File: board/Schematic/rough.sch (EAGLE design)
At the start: 2 parts

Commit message: trying to fix docs glitch
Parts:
- added C1, C2: 10uF, capacitor-wima:C5/3.5
- added C3: 1uF, capacitor-wima:C5/3.5
- added INDUCTOR: INDUCTOR, Test:INDUCTOR
- R1: device rcl:R-EU_M3216 -> resistor:R-US_R1206
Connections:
- new net GND: C1.2, C2.1, U$1.PAD, U$1.TIMER
- new net N$2: C2.2, U$1.BAT
- new net N$3: INDUCTOR.PIN1, R1.1, U$1.SENSE
- new net N$4: C3.1, INDUCTOR.PIN2, U$1.SW
- new net N$5: C3.2, U$1.BOOST
- net N$1: now also C1.1, U$1.SHDN, U$1.VIN; no longer R1.1
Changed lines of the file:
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@@
 <setting verticaltext="up"/>
 </settings>
-<grid distance="0.05" unitdist="mm" unit="mm" style="lines" multiple="1" display="no" altdistance="0.01" altunitdist="inch" altunit="inch"/>
+<grid distance="0.1" unitdist="inch" unit="inch" style="lines" multiple="1" display="yes" altdistance="0.01" altunitdist="inch" altunit="inch"/>
 <layers>
 <layer number="1" name="Top" color="4" fill="1" visible="no" active="no"/>
@@
 <layer number="91" name="Nets" color="2" fill="1" visible="yes" active="yes"/>
 <layer number="92" name="Busses" color="1" fill="1" visible="yes" active="yes"/>
-<layer number="93" name="Pins" color="2" fill="1" visible="yes" active="yes"/>
+<layer number="93" name="Pins" color="2" fill="1" visible="no" active="yes"/>
 <layer number="94" name="Symbols" color="4" fill="1" visible="yes" active="yes"/>
 <layer number="95" name="Names" color="7" fill="1" visible="yes" active="yes"/>
@@
 </classes>
 <parts>
-<part name="U$1" library="Test" deviceset="LT3652" device=""/>
-<part name="R1" library="rcl" deviceset="R-EU_" device="M3216" value="0.05"/>
 <part name="SUPPLY1" library="supply2" deviceset="GND" device=""/>
-<part name="SUPPLY2" library="supply2" deviceset="GND" device=""/>
 <part name="SUPPLY3" library="supply2" deviceset="GND" device=""/>
 <part name="SUPPLY4" library="supply2" deviceset="GND" device=""/>
+<part name="C1" library="capacitor-wima" deviceset="C" device="5/3.5" value="10uF"/>
+<part name="C2" library="capacitor-wima" deviceset="C" device="5/3.5" value="10uF"/>
+<part name="C3" library="capacitor-wima" deviceset="C" device="5/3.5" value="1uF"/>
+<part name="INDUCTOR" library="Test" deviceset="INDUCTOR" device=""/>
+<part name="U$1" library="Test" deviceset="LT3652" device=""/>
+<part name="SUPPLY2" library="supply2" deviceset="GND" device=""/>
+<part name="SUPPLY5" library="supply2" deviceset="GND" device=""/>
+<part name="SUPPLY6" library="supply2" deviceset="GND" device=""/>
+<part name="SUPPLY7" library="supply2" deviceset="GND" device=""/>
+<part name="R1" library="resistor" deviceset="R-US_" device="R1206" value="0.05"/>
 </parts>
 <sheets>
@@
 </plain>
 <instances>
-<instance part="U$1" gate="G$2" x="53.34" y="48.26" rot="R270"/>
-<instance part="R1" gate="G$1" x="85.1" y="50.65"/>
-<instance part="SUPPLY1" gate="GND" x="33.02" y="33.02"/>
-<instance part="SUPPLY2" gate="GND" x="53.49" y="22.95"/>
+<instance part="SUPPLY1" gate="GND" x="12.7" y="73.66"/>
 <instance part="SUPPLY3" gate="GND" x="111.76" y="12.7"/>
-<instance part="SUPPLY4" gate="GND" x="71.12" y="76.2"/>
+<instance part="SUPPLY4" gate="GND" x="35.56" y="45.72"/>
+<instance part="C1" gate="G$1" x="12.7" y="83.82"/>
+<instance part="C2" gate="G$1" x="86.36" y="48.26" rot="R180"/>
+<instance part="C3" gate="G$1" x="78.74" y="71.12"/>
+<instance part="INDUCTOR" gate="G$1" x="93.98" y="71.12" rot="R90"/>
+<instance part="U$1" gate="G$2" x="53.34" y="55.88" rot="R270"/>
+<instance part="SUPPLY2" gate="GND" x="53.34" y="33.02"/>
+<instance part="SUPPLY5" gate="GND" x="53.34" y="25.4"/>
+<instance part="SUPPLY6" gate="GND" x="45.72" y="25.4"/>
+<instance part="SUPPLY7" gate="GND" x="86.36" y="43.18"/>
+<instance part="R1" gate="G$1" x="88.9" y="58.42"/>
 </instances>
 <busses>
@@
 <net name="N$1" class="0">
 <segment>
-<pinref part="R1" gate="G$1" pin="1"/>
-<wire x1="71.12" y1="50.8" x2="80.02" y2="50.65" width="0.1524" layer="91"/>
+<wire x1="12.7" y1="88.9" x2="33.02" y2="88.9" width="0.1524" layer="91"/>
+<pinref part="C1" gate="G$1" pin="1"/>
+<wire x1="33.02" y1="88.9" x2="104.14" y2="88.9" width="0.1524" layer="91"/>
+<wire x1="12.7" y1="86.36" x2="12.7" y2="88.9" width="0.1524" layer="91"/>
+<wire x1="33.02" y1="88.9" x2="33.02" y2="63.5" width="0.1524" layer="91"/>
+<junction x="33.02" y="88.9"/>
+<pinref part="U$1" gate="G$2" pin="SHDN"/>
+<wire x1="33.02" y1="63.5" x2="33.02" y2="58.42" width="0.1524" layer="91"/>
+<wire x1="33.02" y1="58.42" x2="38.1" y2="58.42" width="0.1524" layer="91"/>
+<pinref part="U$1" gate="G$2" pin="VIN"/>
+<wire x1="38.1" y1="63.5" x2="33.02" y2="63.5" width="0.1524" layer="91"/>
+<junction x="33.02" y="63.5"/>
+</segment>
+</net>
+<net name="GND" class="0">
+<segment>
+<pinref part="SUPPLY4" gate="GND" pin="GND"/>
+<pinref part="U$1" gate="G$2" pin="TIMER"/>
+<wire x1="35.56" y1="48.26" x2="38.1" y2="48.26" width="0.1524" layer="91"/>
+</segment>
+<segment>
+<pinref part="SUPPLY1" gate="GND" pin="GND"/>
+<pinref part="C1" gate="G$1" pin="2"/>
+<wire x1="12.7" y1="76.2" x2="12.7" y2="78.74" width="0.1524" layer="91"/>
+</segment>
+<segment>
+<pinref part="U$1" gate="G$2" pin="PAD"/>
+<pinref part="SUPPLY2" gate="GND" pin="GND"/>
+<wire x1="53.34" y1="40.64" x2="53.34" y2="35.56" width="0.1524" layer="91"/>
+</segment>
+<segment>
+<pinref part="C2" gate="G$1" pin="1"/>
+<pinref part="SUPPLY7" gate="GND" pin="GND"/>
 </segment>
 </net>
 <net name="N$2" class="0">
 <segment>
-<wire x1="33" y1="35.6" x2="33" y2="35.9" width="0.1524" layer="91"/>
-<wire x1="33" y1="35.9" x2="36.85" y2="39.75" width="0.1524" layer="91"/>
+<pinref part="U$1" gate="G$2" pin="BAT"/>
+<wire x1="68.58" y1="53.34" x2="86.36" y2="53.34" width="0.1524" layer="91"/>
+<pinref part="C2" gate="G$1" pin="2"/>
+<wire x1="86.36" y1="53.34" x2="93.98" y2="53.34" width="0.1524" layer="91"/>
+<junction x="86.36" y="53.34"/>
 </segment>
 </net>
 <net name="N$3" class="0">
 <segment>
-<wire x1="53.6" y1="26" x2="53.45" y2="26" width="0.1524" layer="91"/>
-<wire x1="53.45" y1="26" x2="53.45" y2="29.75" width="0.1524" layer="91"/>
+<pinref part="U$1" gate="G$2" pin="SENSE"/>
+<pinref part="R1" gate="G$1" pin="1"/>
+<wire x1="68.58" y1="58.42" x2="81.28" y2="58.42" width="0.1524" layer="91"/>
+<pinref part="INDUCTOR" gate="G$1" pin="PIN1"/>
+<wire x1="81.28" y1="58.42" x2="83.82" y2="58.42" width="0.1524" layer="91"/>
+<wire x1="86.36" y1="68.58" x2="81.28" y2="63.5" width="0.1524" layer="91"/>
+<wire x1="81.28" y1="63.5" x2="81.28" y2="58.42" width="0.1524" layer="91"/>
+<junction x="81.28" y="58.42"/>
 </segment>
 </net>
+<net name="N$4" class="0">
+<segment>
+<pinref part="U$1" gate="G$2" pin="SW"/>
+<pinref part="C3" gate="G$1" pin="1"/>
+<wire x1="68.58" y1="63.5" x2="68.58" y2="73.66" width="0.1524" layer="91"/>
+<wire x1="68.58" y1="73.66" x2="78.74" y2="73.66" width="0.1524" layer="91"/>
+<pinref part="INDUCTOR" gate="G$1" pin="PIN2"/>
+<wire x1="78.74" y1="73.66" x2="86.36" y2="73.66" width="0.1524" layer="91"/>
+<junction x="78.74" y="73.66"/>
+</segment>
+</net>
+<net name="N$5" class="0">
+<segment>
+<pinref part="U$1" gate="G$2" pin="BOOST"/>
+<pinref part="C3" gate="G$1" pin="2"/>
+<wire x1="68.58" y1="60.96" x2="78.74" y2="66.04" width="0.1524" layer="91"/>
+</segment>
+</net>

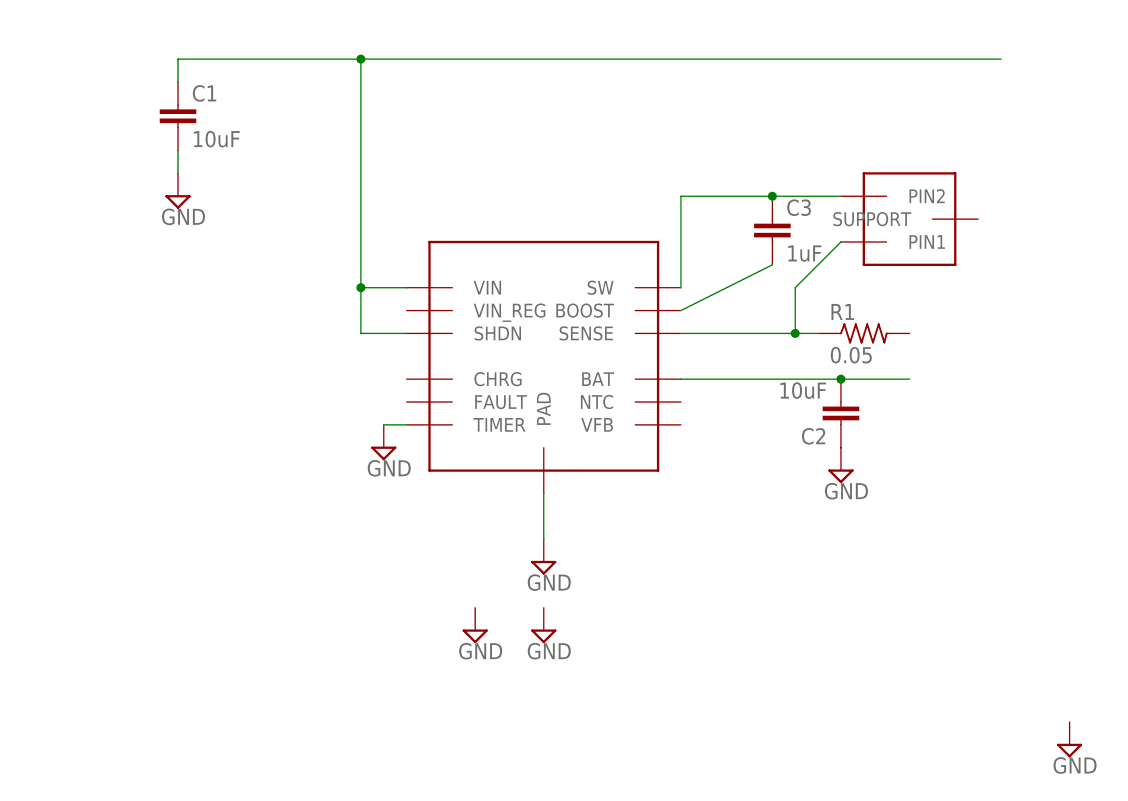
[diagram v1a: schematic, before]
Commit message: diodes added
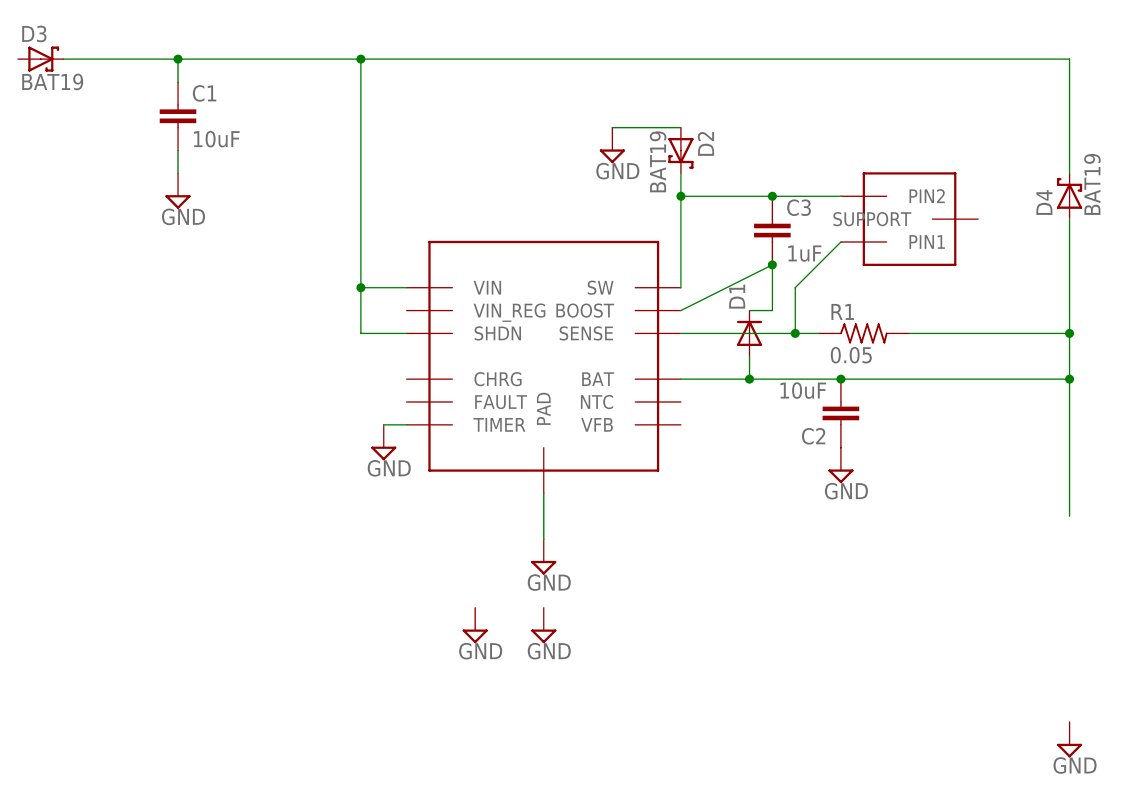
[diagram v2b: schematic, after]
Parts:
- added D1: (no value), diode:DIODE-SOD80C
- added D2, D3, D4: BAT19, diode:BAT19
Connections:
- net GND: now also D2.A
- net N$1: now also D3.C, D4.C
- net N$2: now also D1.A, D4.A, R1.2
- net N$4: now also D2.C
- net N$5: now also D1.C
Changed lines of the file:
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@@
 <setting verticaltext="up"/>
 </settings>
-<grid distance="0.1" unitdist="inch" unit="inch" style="lines" multiple="1" display="yes" altdistance="0.01" altunitdist="inch" altunit="inch"/>
+<grid distance="0.1" unitdist="inch" unit="inch" style="lines" multiple="1" display="no" altdistance="0.01" altunitdist="inch" altunit="inch"/>
 <layers>
 <layer number="1" name="Top" color="4" fill="1" visible="no" active="no"/>
@@
 <part name="SUPPLY7" library="supply2" deviceset="GND" device=""/>
 <part name="R1" library="resistor" deviceset="R-US_" device="R1206" value="0.05"/>
+<part name="D2" library="diode" deviceset="BAT19" device=""/>
+<part name="SUPPLY8" library="supply2" deviceset="GND" device=""/>
+<part name="D1" library="diode" deviceset="DIODE-" device="SOD80C"/>
+<part name="D3" library="diode" deviceset="BAT19" device=""/>
+<part name="D4" library="diode" deviceset="BAT19" device=""/>
 </parts>
 <sheets>
@@
 <instance part="SUPPLY7" gate="GND" x="86.36" y="43.18"/>
 <instance part="R1" gate="G$1" x="88.9" y="58.42"/>
+<instance part="D2" gate="1" x="68.58" y="78.74" rot="R270"/>
+<instance part="SUPPLY8" gate="GND" x="60.96" y="78.74"/>
+<instance part="D1" gate="G$1" x="76.2" y="58.42" rot="R90"/>
+<instance part="D3" gate="1" x="-2.54" y="88.9"/>
+<instance part="D4" gate="1" x="111.76" y="73.66" rot="R90"/>
 </instances>
 <busses>
@@
 <wire x1="12.7" y1="88.9" x2="33.02" y2="88.9" width="0.1524" layer="91"/>
 <pinref part="C1" gate="G$1" pin="1"/>
-<wire x1="33.02" y1="88.9" x2="104.14" y2="88.9" width="0.1524" layer="91"/>
+<wire x1="33.02" y1="88.9" x2="111.76" y2="88.9" width="0.1524" layer="91"/>
 <wire x1="12.7" y1="86.36" x2="12.7" y2="88.9" width="0.1524" layer="91"/>
 <wire x1="33.02" y1="88.9" x2="33.02" y2="63.5" width="0.1524" layer="91"/>
@@
 <wire x1="38.1" y1="63.5" x2="33.02" y2="63.5" width="0.1524" layer="91"/>
 <junction x="33.02" y="63.5"/>
+<pinref part="D4" gate="1" pin="C"/>
+<wire x1="111.76" y1="76.2" x2="111.76" y2="88.9" width="0.1524" layer="91"/>
+<pinref part="D3" gate="1" pin="C"/>
+<wire x1="0" y1="88.9" x2="12.7" y2="88.9" width="0.1524" layer="91"/>
+<junction x="12.7" y="88.9"/>
 </segment>
 </net>
@@
 <pinref part="SUPPLY7" gate="GND" pin="GND"/>
 </segment>
+<segment>
+<pinref part="D2" gate="1" pin="A"/>
+<pinref part="SUPPLY8" gate="GND" pin="GND"/>
+<wire x1="68.58" y1="81.28" x2="60.96" y2="81.28" width="0.1524" layer="91"/>
+</segment>
 </net>
 <net name="N$2" class="0">
 <segment>
 <pinref part="U$1" gate="G$2" pin="BAT"/>
-<wire x1="68.58" y1="53.34" x2="86.36" y2="53.34" width="0.1524" layer="91"/>
+<wire x1="68.58" y1="53.34" x2="76.2" y2="53.34" width="0.1524" layer="91"/>
 <pinref part="C2" gate="G$1" pin="2"/>
-<wire x1="86.36" y1="53.34" x2="93.98" y2="53.34" width="0.1524" layer="91"/>
+<wire x1="76.2" y1="53.34" x2="86.36" y2="53.34" width="0.1524" layer="91"/>
 <junction x="86.36" y="53.34"/>
+<pinref part="D1" gate="G$1" pin="A"/>
+<wire x1="76.2" y1="55.88" x2="76.2" y2="53.34" width="0.1524" layer="91"/>
+<junction x="76.2" y="53.34"/>
+<pinref part="D4" gate="1" pin="A"/>
+<wire x1="111.76" y1="71.12" x2="111.76" y2="58.42" width="0.1524" layer="91"/>
+<pinref part="R1" gate="G$1" pin="2"/>
+<wire x1="111.76" y1="58.42" x2="111.76" y2="53.34" width="0.1524" layer="91"/>
+<wire x1="111.76" y1="53.34" x2="111.76" y2="38.1" width="0.1524" layer="91"/>
+<wire x1="93.98" y1="58.42" x2="111.76" y2="58.42" width="0.1524" layer="91"/>
+<junction x="111.76" y="58.42"/>
+<wire x1="86.36" y1="53.34" x2="111.76" y2="53.34" width="0.1524" layer="91"/>
+<junction x="111.76" y="53.34"/>
 </segment>
 </net>
@@
 <wire x1="78.74" y1="73.66" x2="86.36" y2="73.66" width="0.1524" layer="91"/>
 <junction x="78.74" y="73.66"/>
+<pinref part="D2" gate="1" pin="C"/>
+<wire x1="68.58" y1="76.2" x2="68.58" y2="73.66" width="0.1524" layer="91"/>
+<junction x="68.58" y="73.66"/>
 </segment>
 </net>
@@
 <pinref part="C3" gate="G$1" pin="2"/>
 <wire x1="68.58" y1="60.96" x2="78.74" y2="66.04" width="0.1524" layer="91"/>
-</segment>
-</net>
+<pinref part="D1" gate="G$1" pin="C"/>
+<wire x1="76.2" y1="60.96" x2="78.74" y2="60.96" width="0.1524" layer="91"/>
+<wire x1="78.74" y1="60.96" x2="78.74" y2="66.04" width="0.1524" layer="91"/>
+<junction x="78.74" y="66.04"/>
+</segment>
+</net>

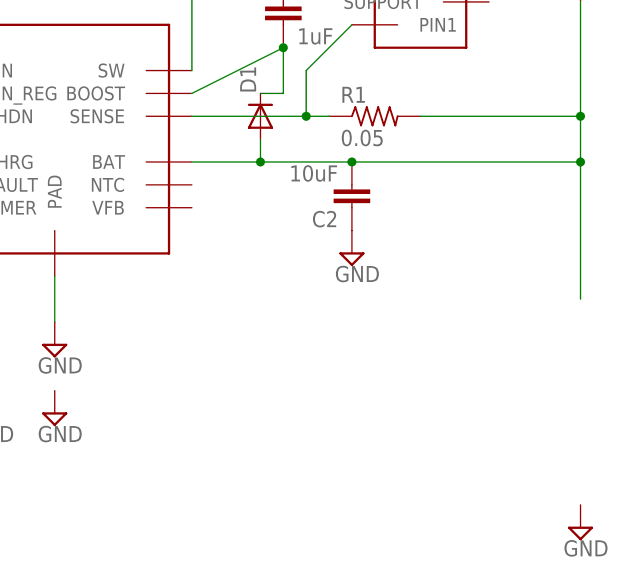
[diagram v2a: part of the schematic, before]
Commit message: added resistors
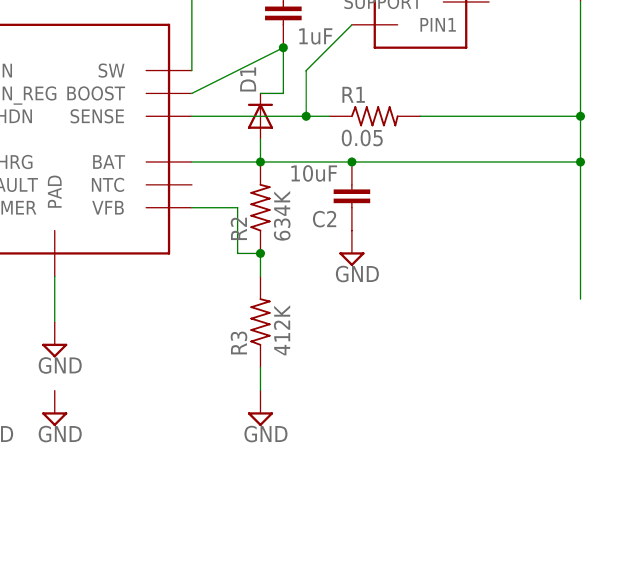
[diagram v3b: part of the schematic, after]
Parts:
- added R2: 634K, rcl:R-US_M2012
- added R3: 412K, rcl:R-US_M2012
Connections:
- new net N$6: R2.1, R3.2, U$1.VFB
- net GND: now also R3.1
- net N$2: now also R2.2
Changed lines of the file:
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@@
 <part name="D3" library="diode" deviceset="BAT19" device=""/>
 <part name="D4" library="diode" deviceset="BAT19" device=""/>
+<part name="R2" library="rcl" deviceset="R-US_" device="M2012" value="634K"/>
+<part name="R3" library="rcl" deviceset="R-US_" device="M2012" value="412K"/>
 </parts>
 <sheets>
@@
 <instances>
 <instance part="SUPPLY1" gate="GND" x="12.7" y="73.66"/>
-<instance part="SUPPLY3" gate="GND" x="111.76" y="12.7"/>
+<instance part="SUPPLY3" gate="GND" x="76.2" y="25.4"/>
 <instance part="SUPPLY4" gate="GND" x="35.56" y="45.72"/>
 <instance part="C1" gate="G$1" x="12.7" y="83.82"/>
@@
 <instance part="D3" gate="1" x="-2.54" y="88.9"/>
 <instance part="D4" gate="1" x="111.76" y="73.66" rot="R90"/>
+<instance part="R2" gate="G$1" x="76.2" y="48.26" rot="R90"/>
+<instance part="R3" gate="G$1" x="76.2" y="35.56" rot="R90"/>
 </instances>
 <busses>
@@
 <wire x1="68.58" y1="81.28" x2="60.96" y2="81.28" width="0.1524" layer="91"/>
 </segment>
+<segment>
+<pinref part="SUPPLY3" gate="GND" pin="GND"/>
+<pinref part="R3" gate="G$1" pin="1"/>
+<wire x1="76.2" y1="27.94" x2="76.2" y2="30.48" width="0.1524" layer="91"/>
+</segment>
 </net>
 <net name="N$2" class="0">
@@
 <wire x1="86.36" y1="53.34" x2="111.76" y2="53.34" width="0.1524" layer="91"/>
 <junction x="111.76" y="53.34"/>
+<pinref part="R2" gate="G$1" pin="2"/>
 </segment>
 </net>
@@
 </segment>
 </net>
+<net name="N$6" class="0">
+<segment>
+<pinref part="R2" gate="G$1" pin="1"/>
+<wire x1="76.2" y1="43.18" x2="73.66" y2="43.18" width="0.1524" layer="91"/>
+<wire x1="73.66" y1="43.18" x2="73.66" y2="48.26" width="0.1524" layer="91"/>
+<pinref part="U$1" gate="G$2" pin="VFB"/>
+<wire x1="73.66" y1="48.26" x2="68.58" y2="48.26" width="0.1524" layer="91"/>
+<pinref part="R3" gate="G$1" pin="2"/>
+<wire x1="76.2" y1="40.64" x2="76.2" y2="43.18" width="0.1524" layer="91"/>
+<junction x="76.2" y="43.18"/>
+</segment>
+</net>
